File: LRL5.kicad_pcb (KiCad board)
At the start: 2 copper layers, 140 x 50 mm, 33 parts, among them J1 POWER, J2 On/Off, J5 OUT, J6 MODE, J7 ADJUST, Q1 BC549, U1 BA033CC0T, U2 NHD-C0220BIZ

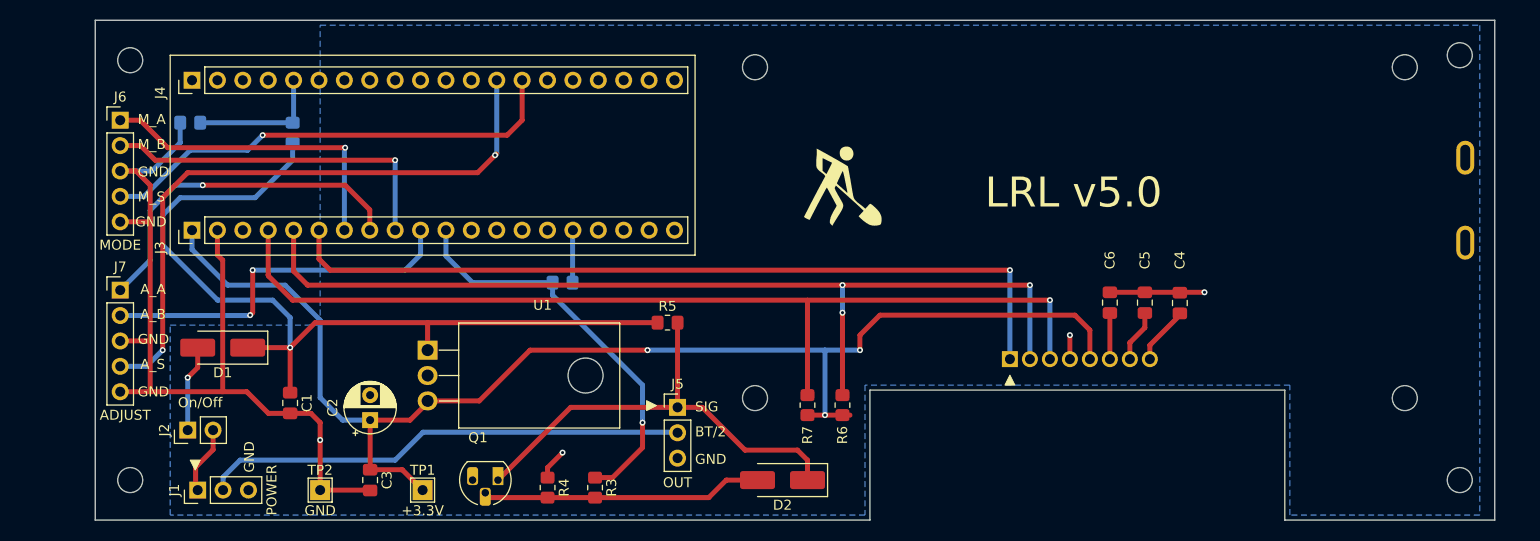
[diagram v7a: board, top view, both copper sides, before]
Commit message: Redesign board. Move connectors
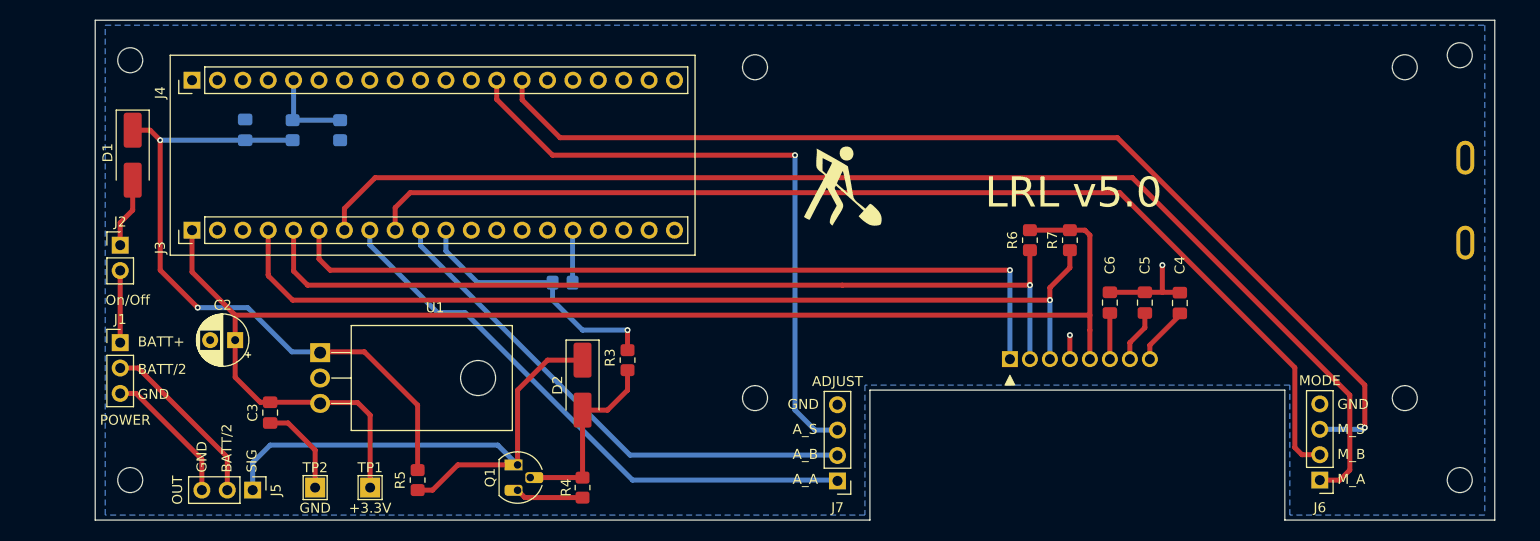
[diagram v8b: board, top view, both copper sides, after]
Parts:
- C1: moved to B.Cu
- H1, H2, H3, H4: value Hole -> MountingHole
- J6, J7: footprint Connector_PinHeader_2.54mm:PinHeader_1x05_P2.54mm_Vertical -> Connector_PinHeader_2.54mm:PinHeader_1x04_P2.54mm_Vertical
- moved J6 125.3 mm to (250.0, 76.0), turned to 180 degrees
- moved J7 74.2 mm to (201.8, 76.1), turned to 180 degrees
- moved J5 43.3 mm to (143.2, 77.0), turned to -90 degrees
- moved R7 31.0 mm to (225.0, 52.0), turned to -90 degrees
- moved R5 29.5 mm to (159.8, 76.0), turned to -90 degrees
- moved C1 27.7 mm to (142.5, 41.0), turned to 90 degrees
- moved R6 25.0 mm to (221.0, 52.0), turned to -90 degrees
- moved D2 22.1 mm to (176.2, 66.5), turned to -90 degrees
- moved D1 21.2 mm to (131.2, 43.5), turned to -90 degrees
- moved J2 19.7 mm to (130.0, 52.5), turned to 0 degrees
- moved J1 16.7 mm to (130.0, 62.2), turned to 0 degrees
- moved C2 15.7 mm to (141.5, 62.0), turned to 180 degrees
- moved R2 15.0 mm to (152.0, 41.0), turned to -90 degrees
- moved R3 13.2 mm to (180.8, 64.0)
- moved C3 12.1 mm to (145.0, 69.2)
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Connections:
- J6 pad 3: GND -> MODE_SW1
- J6 pad 4: MODE_SW1 -> GND
- J7 pad 3: GND -> ADJUST_SW1
- J7 pad 4: ADJUST_SW1 -> GND
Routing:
- net MODE_A: track 31.9 -> 123.9 mm, vias 1 -> 0
- net MODE_B: track 35.1 -> 110.9 mm, vias 1 -> 0
- net GND: track 105.1 -> 43.2 mm, vias 4 -> 2
- net MODE_SW1: track 47.4 -> 107.0 mm
- net BATT/2: track 48.4 -> 17.7 mm
- net ADJUST_A: track 35.3 -> 58.0 mm, vias 1 -> 0
- net +BATT: track 88.1 -> 67.3 mm, vias 1 -> 2
- net ADJUST_B: track 37.5 -> 51.9 mm, vias 2 -> 0
- net FOUT: track 40.6 -> 26.6 mm
- net Net-(D2-K): track 46.6 -> 57.1 mm
- net Net-(D2-A): track 28.2 -> 19.3 mm
- net +3.3V: track 134.4 -> 143.0 mm, vias 3 -> 0
- net I2C1_SCL: track 96.8 -> 89.3 mm, vias 3 -> 1
- net VBAT: track 13.8 -> 9.14 mm
- net I2C1_SDA: track 99.2 -> 95.5 mm
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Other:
- board text added: "BATT+"
- board text added: "BATT/2"
- board text removed: "BT/2"
- board text removed: "I2C1_SDA"
